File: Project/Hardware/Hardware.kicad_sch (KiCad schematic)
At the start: 20 parts, among them SW1 SW_Push, SW2 SW_Push, SW3 SW_Push, U1 LCD1602_I2C, U2 HM-10, U3 DS3231M

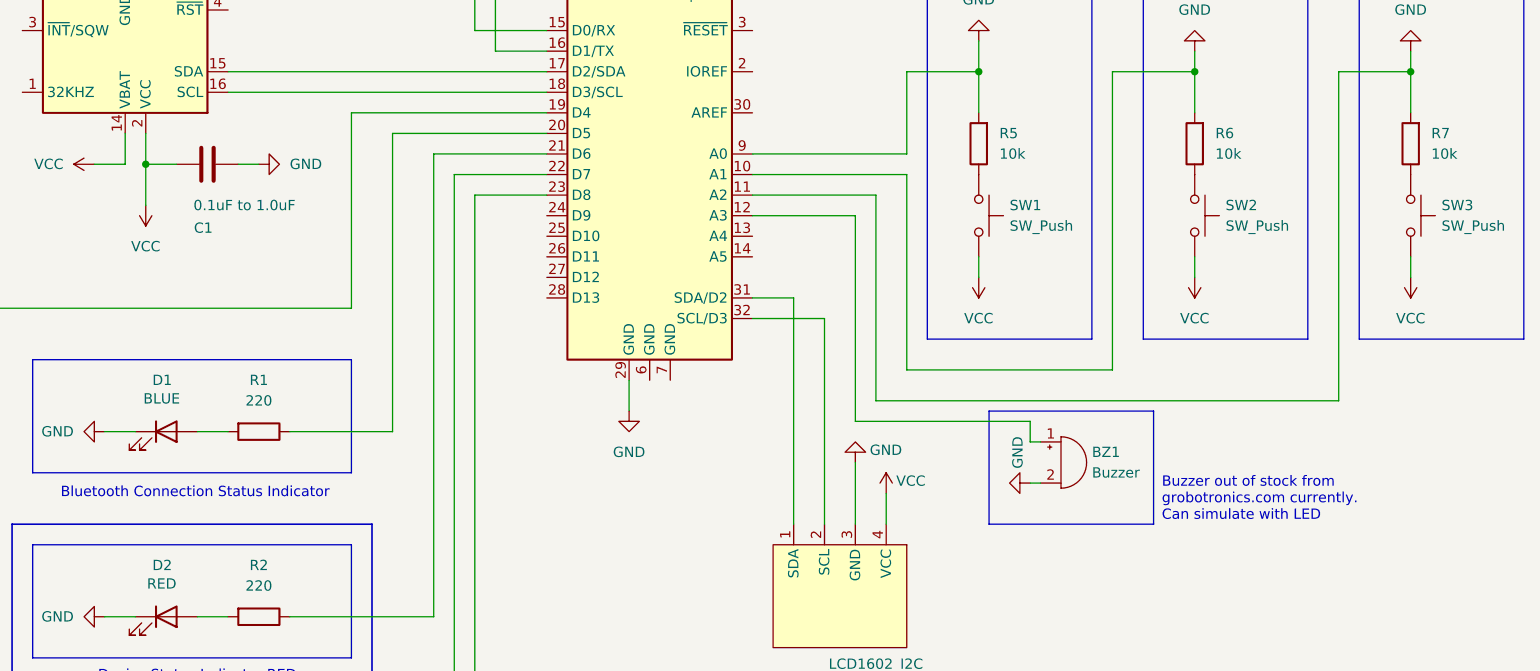
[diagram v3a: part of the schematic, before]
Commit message: Change C1 capacitor from unpolarised to polarised
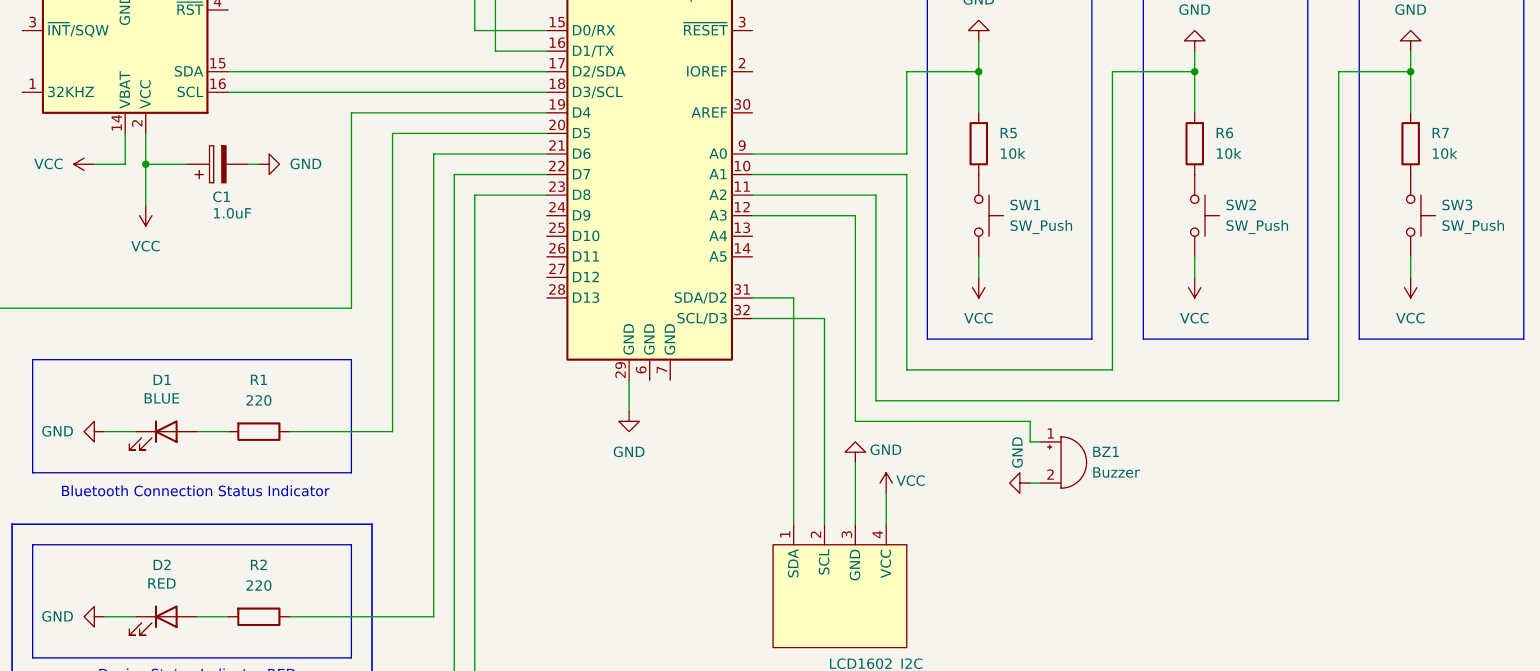
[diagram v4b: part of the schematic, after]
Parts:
- removed C1: 0.1uF to 1.0uF, symbol Device:C
- added C1: 1.0uF, symbol Device:C_Polarized
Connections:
- net GND: now also C1.2
- net VCC: now also C1.1
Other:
- note removed: "Buzzer out of stock from grobotronics.com currently. Can simulate with LED"
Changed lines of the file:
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@@
-	)
-	(rectangle
-		(start 193.04 109.22)
-		(end 213.36 123.19)
-		(stroke
-			(width 0)
-			(type default)
-		)
-		(fill
-			(type none)
-		)
 	)
 	(rectangle
@@
 		)
 	)
-	(text "Buzzer out of stock from\ngrobotronics.com currently.\nCan simulate with LED"
-		(exclude_from_sim no)
-		(at 214.376 120.142 0)
-		(effects
-			(font
-				(size 1.27 1.27)
-			)
-			(justify left)
-		)
-	)
 	(text "MENU_BTN_SELECT"
 		(exclude_from_sim no)
@@
 	(wire
 		(pts
+			(xy 176.53 110.49) (xy 198.12 110.49)
+		)
+		(stroke
+			(width 0)
+			(type default)
+		)
+	)
+	(wire
+		(pts
+			(xy 208.28 67.31) (xy 218.44 67.31)
+		)
+		(stroke
+			(width 0)
+			(type default)
+		)
+	)
+	(wire
+		(pts
 			(xy 88.9 74.93) (xy 88.9 78.74)
 		)
@@
 	(wire
 		(pts
-			(xy 176.53 110.49) (xy 198.12 110.49)
-		)
-		(stroke
-			(width 0)
-			(type default)
-		)
-	)
-	(wire
-		(pts
-			(xy 208.28 67.31) (xy 218.44 67.31)
-		)
-		(stroke
-			(width 0)
-			(type default)
-		)
-	)
-	(wire
-		(pts
 			(xy 127 80.01) (xy 138.43 80.01)
 		)
@@
 	(wire
 		(pts
-			(xy 100.33 78.74) (xy 102.87 78.74)
+			(xy 101.6 78.74) (xy 102.87 78.74)
 		)
 		(stroke
@@
 	(wire
 		(pts
+			(xy 88.9 78.74) (xy 88.9 83.82)
+		)
+		(stroke
+			(width 0)
+			(type default)
+		)
+	)
+	(wire
+		(pts
 			(xy 129.54 172.72) (xy 129.54 82.55)
 		)
@@
 	(wire
 		(pts
-			(xy 88.9 78.74) (xy 92.71 78.74)
+			(xy 88.9 78.74) (xy 93.98 78.74)
 		)
 		(stroke
@@
 		(pts
 			(xy 132.08 44.45) (xy 132.08 64.77)
-		)
-		(stroke
-			(width 0)
-			(type default)
-		)
-	)
-	(wire
-		(pts
-			(xy 88.9 78.74) (xy 88.9 83.82)
 		)
 		(stroke
@@
 	)
 	(symbol
+		(lib_id "Device:C_Polarized")
+		(at 97.79 78.74 90)
+		(unit 1)
+		(exclude_from_sim no)
+		(in_bom yes)
+		(on_board yes)
+		(dnp no)
+		(property "Reference" "C1"
+			(at 98.298 82.804 90)
+			(effects
+				(font
+					(size 1.27 1.27)
+				)
+			)
+		)
+		(property "Value" "1.0uF"
+			(at 99.568 84.836 90)
+			(effects
+				(font
+					(size 1.27 1.27)
+				)
+			)
+		)
+		(property "Footprint" ""
+			(at 101.6 77.7748 0)
+			(effects
+				(font
+					(size 1.27 1.27)
+				)
+				(hide yes)
+			)
+		)
+		(property "Datasheet" "~"
+			(at 97.79 78.74 0)
+			(effects
+				(font
+					(size 1.27 1.27)
+				)
+				(hide yes)
+			)
+		)
+		(property "Description" "Polarized capacitor"
+			(at 97.79 78.74 0)
+			(effects
+				(font
+					(size 1.27 1.27)
+				)
+				(hide yes)
+			)
+		)
+		(pin "2"
+		)
+		(pin "1"
+		)
+		(instances
+			(project ""
+				(path "/823843db-cbc4-413a-a2ac-ffbd107e023e"
+					(reference "C1")
+					(unit 1)
+				)
+			)
+		)
+	)
+	(symbol
 		(lib_id "Device:R")
 		(at 191.77 76.2 180)
@@
 					(unit 1)
 				)
-			)
-		)
-	)
-	(symbol
-		(lib_id "Device:C")
-		(at 96.52 78.74 90)
-		(unit 1)
-		(exclude_from_sim no)
-		(in_bom yes)
-		(on_board yes)
-		(dnp no)
-		(property "Reference" "C1"
-			(at 96.012 86.614 90)
-			(effects
-				(font
-					(size 1.27 1.27)
-				)
-			)
-		)
-		(property "Value" "0.1uF to 1.0uF"
-			(at 101.092 83.82 90)
-			(effects
-				(font
-					(size 1.27 1.27)
-				)
-			)
-		)
-		(property "Footprint" ""
-			(at 100.33 77.7748 0)
-			(effects
-				(font
-					(size 1.27 1.27)
-				)
-				(hide yes)
-			)
-		)
-		(property "Datasheet" "~"
-			(at 96.52 78.74 0)
-			(effects
-				(font
-					(size 1.27 1.27)
-				)
-				(hide yes)
-			)
-		)
-		(property "Description" "Unpolarized capacitor"
-			(at 96.52 78.74 0)
-			(effects
-				(font
-					(size 1.27 1.27)
-				)
-				(hide yes)
-			)
-		)
-		(pin "1"
-		)
-		(pin "2"
-		)
-		(instances
-			(project ""
-				(path "/823843db-cbc4-413a-a2ac-ffbd107e023e"
-					(reference "C1")
-					(unit 1)
-				)

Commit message: Change polarised capacitor to unpolarised in schematic and setup LaTeX references
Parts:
- removed C1: 1.0uF, symbol Device:C_Polarized
- added C2: 0.1uF to 1.0uF, symbol Device:C
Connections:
- net GND: now also C2.2
- net VCC: now also C2.1

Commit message: Add modified version of waveshare lcd1602 arduino library
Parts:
- renumbered C2 to C1
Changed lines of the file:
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@@
 		(on_board yes)
 		(dnp no)
-		(property "Reference" "C2"
+		(property "Reference" "C1"
 			(at 97.79 83.82 90)
 			(effects
@@
 			(project ""
 				(path "/823843db-cbc4-413a-a2ac-ffbd107e023e"
-					(reference "C2")
+					(reference "C1")
 					(unit 1)
 				)

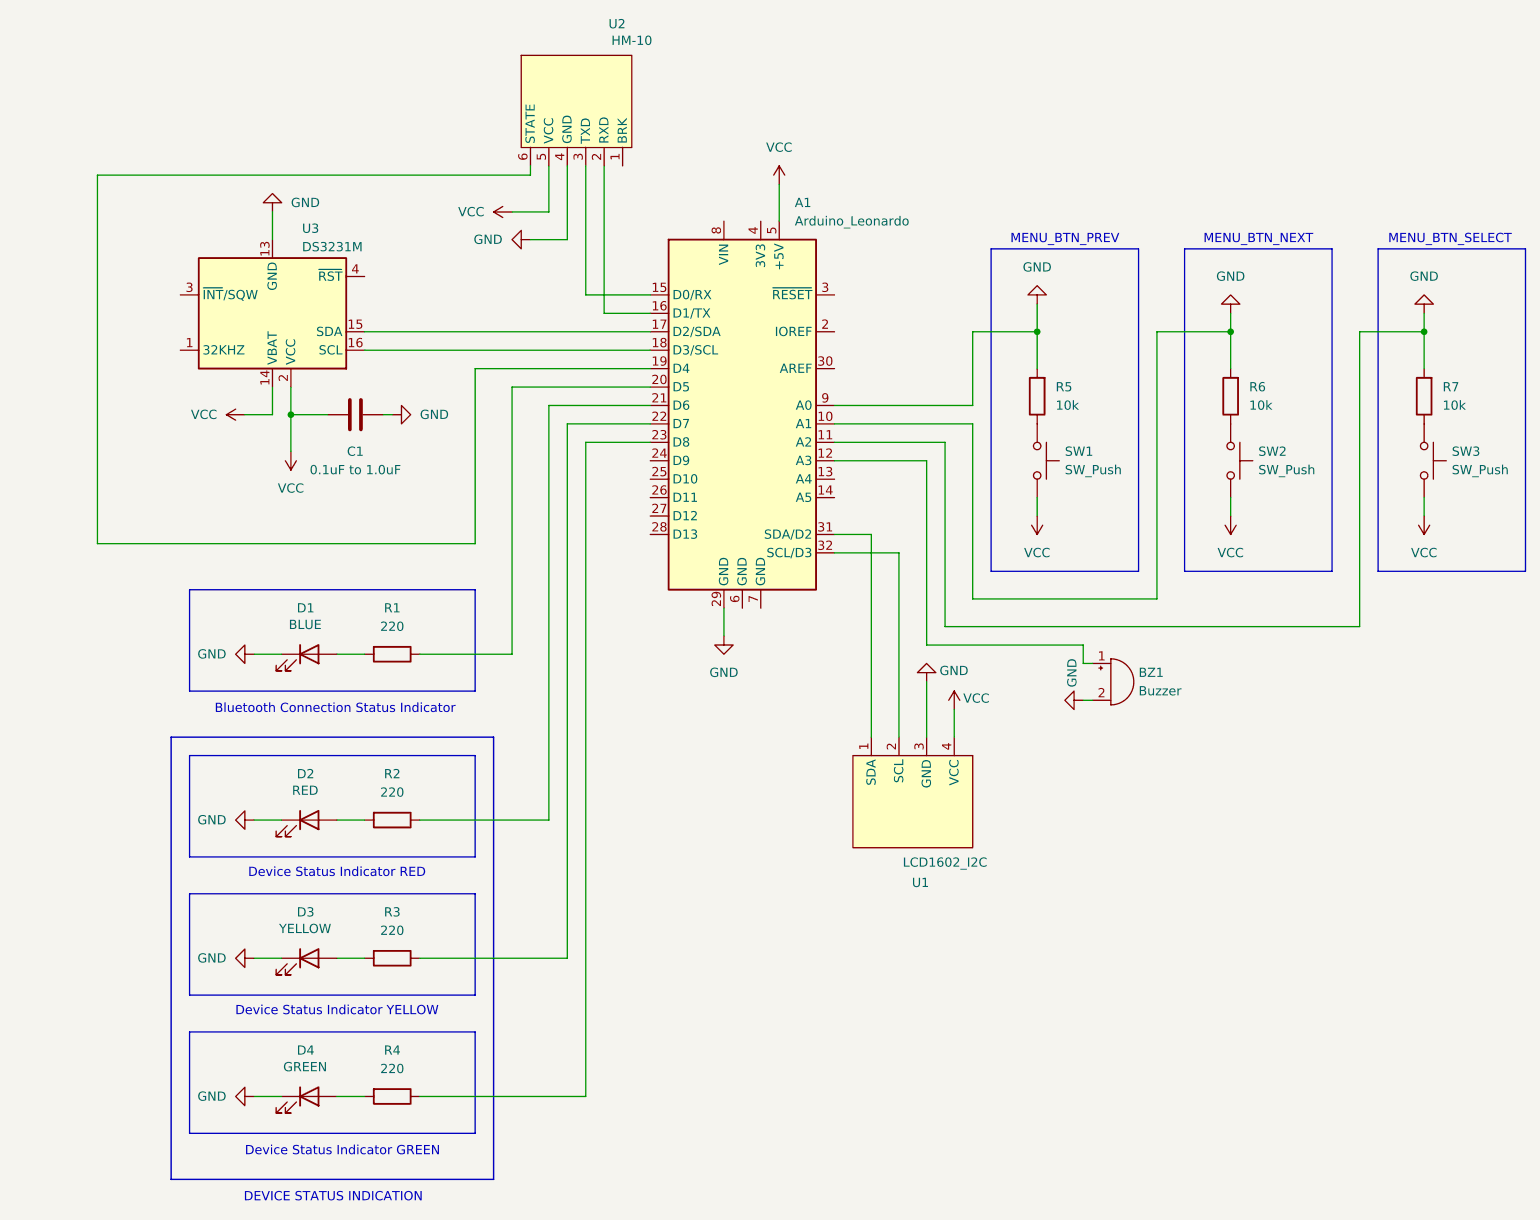
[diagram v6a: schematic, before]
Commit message: Update schematic to follow actual pin configuration
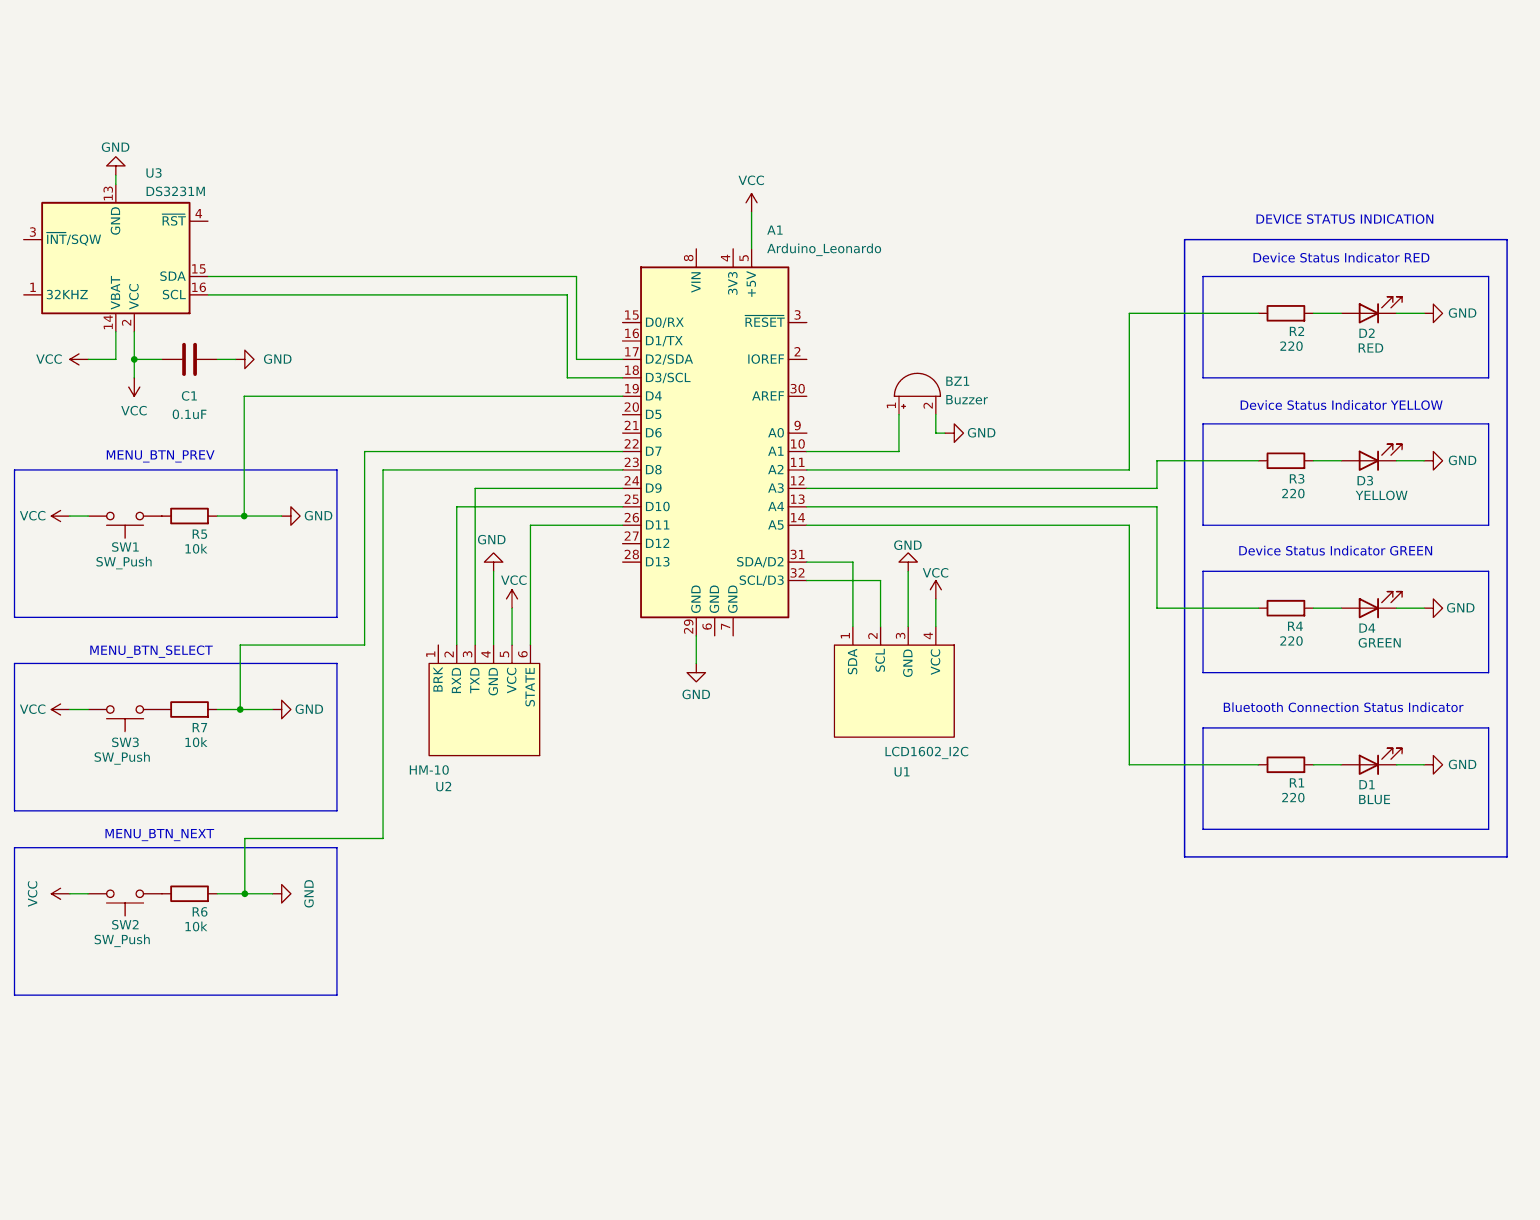
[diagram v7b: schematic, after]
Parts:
- C1: value 0.1uF to 1.0uF -> 0.1uF
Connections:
- net GND: now also A1.19 (D4), A1.22 (D7), A1.23 (D8); no longer A1.10 (A1), A1.11 (A2), A1.9 (A0)
- net at R4.1: now also A1.13 (A4); no longer A1.23 (D8)
- net at R2.1: now also A1.11 (A2); no longer A1.21 (D6)
- net at R3.1: now also A1.12 (A3); no longer A1.22 (D7)
- net at BZ1.1 (+): now also A1.10 (A1); no longer A1.12 (A3)
- net at R1.1: now also A1.14 (A5); no longer A1.20 (D5)
- net at A1.15 (D0/RX): no longer U2.3 (TXD)
- net at A1.16 (D1/TX): no longer U2.2 (RXD)
- net at U2.6 (STATE): now also A1.26 (D11); no longer A1.19 (D4)
- net at A1.24 (D9): now also U2.3 (TXD)
- net at A1.25 (D10): now also U2.2 (RXD)
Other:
- moved on the sheet: A1, BZ1, C1, D1, D2, D3, D4, R1, R2, R3, R4, R5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
